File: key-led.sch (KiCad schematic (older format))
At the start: 8 parts, among them J1 Conn_01x01_Female, J2 Conn_01x01_Female, J3 Conn_01x01_Female, J4 Conn_01x01_Female, J5 Conn_01x01_Female, J6 Conn_01x01_Female, SW1 SW_Push_45deg

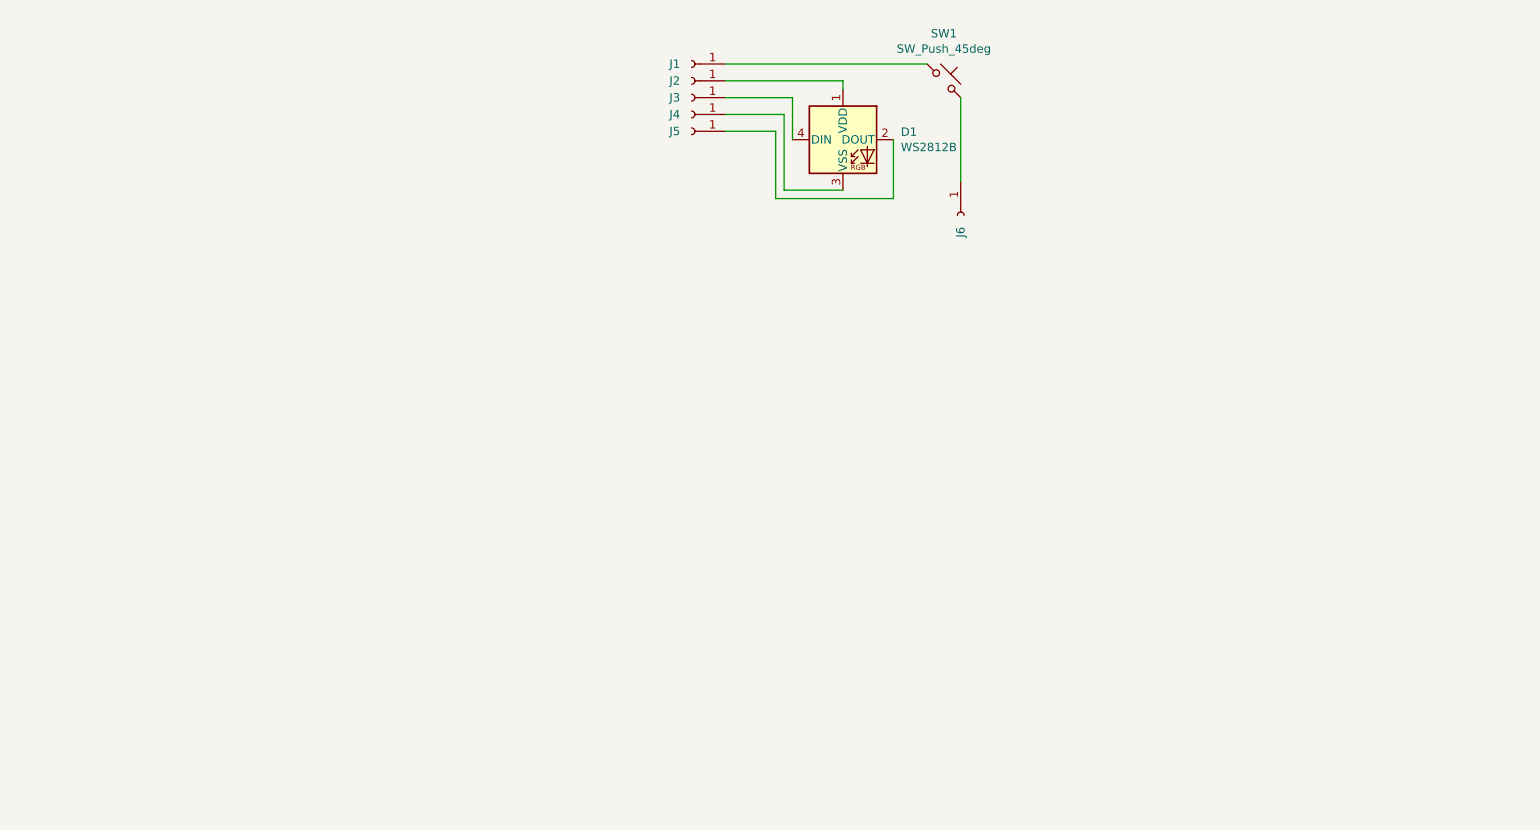
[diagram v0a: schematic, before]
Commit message: 4x row design, layout and route
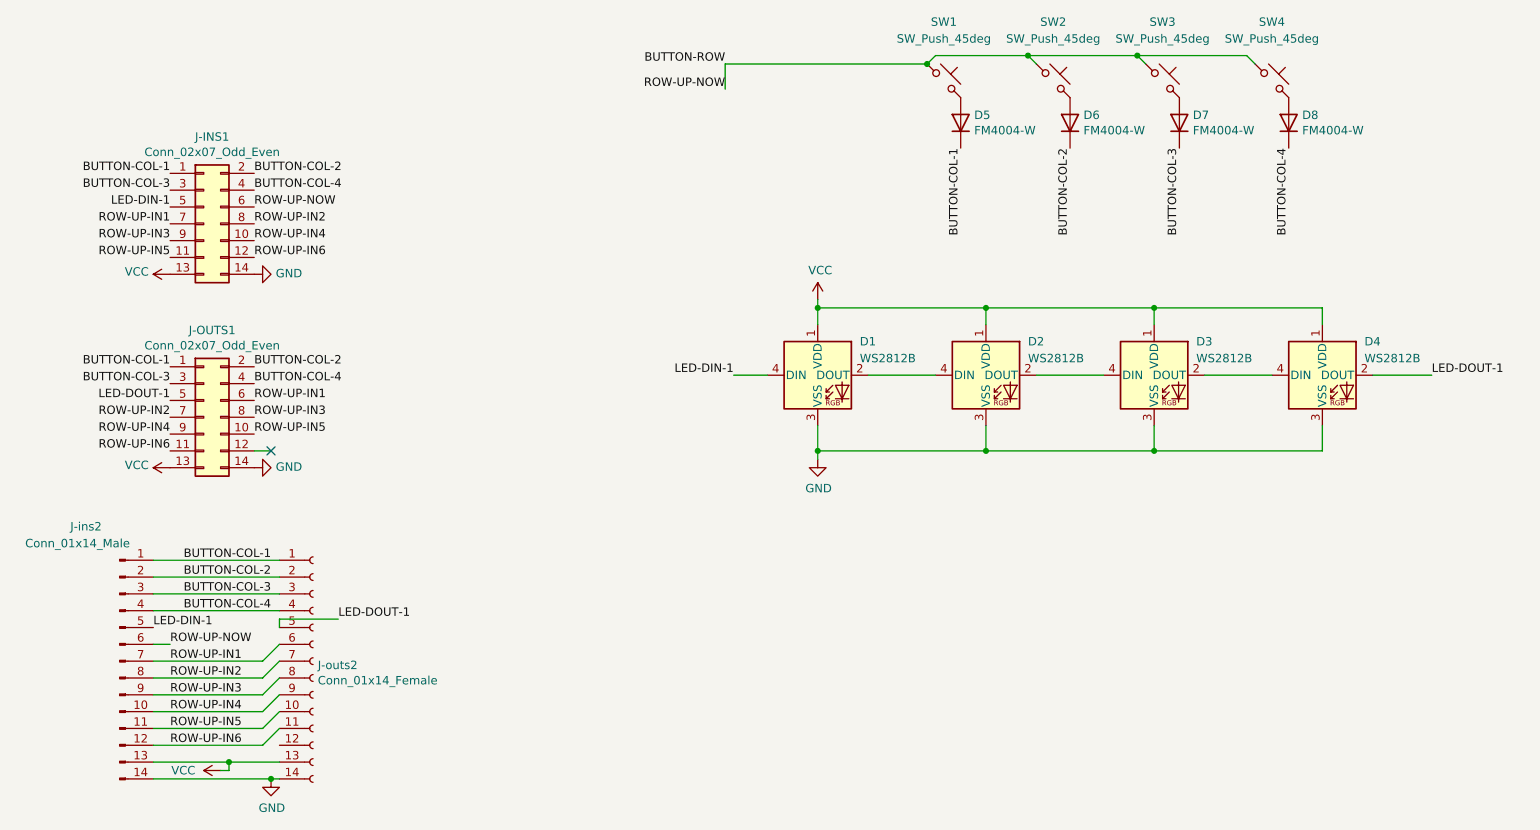
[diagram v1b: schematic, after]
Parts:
- removed J1, J2, J3, J4, J5, J6: Conn_01x01_Female, Connector_Pin:Pin_D0.9mm_L10.0mm_W2.4mm_FlatFork, symbol Connector:Conn_01x01_Female
- added D2, D3, D4: WS2812B, key-led:LED_WS2812B_PLCC4-back-mount, symbol LED:WS2812B
- added D5, D6, D7, D8: FM4004-W, Diode_SMD:D_SMA_Handsoldering, symbol Device:D
- added J-INS1, J-OUTS1: Conn_02x07_Odd_Even, Connector_PinHeader_2.54mm:PinHeader_2x07_P2.54mm_Vertical, symbol Connector_Generic:Conn_02x07_Odd_Even
- added J-ins2: Conn_01x14_Male, Connector_PinHeader_2.54mm:PinHeader_1x14_P2.54mm_Vertical, symbol Connector:Conn_01x14_Male
- added J-outs2: Conn_01x14_Female, Connector_PinHeader_2.54mm:PinHeader_1x14_P2.54mm_Vertical, symbol Connector:Conn_01x14_Female
- added SW2, SW3, SW4: SW_Push_45deg, key-led:SW_Cherry_MX_1.00u_PCB, symbol Switch:SW_Push_45deg
- D1: footprint LED_SMD:LED_WS2812B_PLCC4_5.0x5.0mm_P3.2mm -> key-led:LED_WS2812B_PLCC4-back-mount; buy link (none) -> https://www.ebay.com/itm/WS2812B-5050-SMD-Individually-Addr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
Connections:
- net VCC: now reaches D1.1 (VDD)
- net VCC: now also D2.1 (VDD), D3.1 (VDD), D4.1 (VDD), J-INS1.13 (Pin_13), J-OUTS1.13 (Pin_13), J-ins2.13 (Pin_13), J-outs2.13 (Pin_13)
- net at D1.2 (DOUT): now also D2.4 (DIN)
- net GND: now reaches D1.3 (VSS)
- net GND: now also D2.3 (VSS), D3.3 (VSS), D4.3 (VSS), J-INS1.14 (Pin_14), J-OUTS1.14 (Pin_14), J-ins2.14 (Pin_14), J-outs2.14 (Pin_14)
- net LED-DIN-1: now reaches D1.4 (DIN)
- net LED-DIN-1: now also J-INS1.5 (Pin_5), J-ins2.5 (Pin_5)
- net BUTTON-ROW: now reaches SW1.1
- net BUTTON-ROW: now also J-INS1.6 (Pin_6), J-ins2.6 (Pin_6), SW2.1, SW3.1, SW4.1
- net at SW1.2: now also D5.2 (A)
- new net: D6.2 (A), SW2.2
- new net: D7.2 (A), SW3.2
- new net: D8.2 (A), SW4.2
- new net: D2.2 (DOUT), D3.4 (DIN)
- new net: D3.2 (DOUT), D4.4 (DIN)
- new net BUTTON-COL-1: D5.1 (K), J-INS1.1 (Pin_1), J-OUTS1.1 (Pin_1), J-ins2.1 (Pin_1), J-outs2.1 (Pin_1)
- new net BUTTON-COL-2: D6.1 (K), J-INS1.2 (Pin_2), J-OUTS1.2 (Pin_2), J-ins2.2 (Pin_2), J-outs2.2 (Pin_2)
- new net BUTTON-COL-3: D7.1 (K), J-INS1.3 (Pin_3), J-OUTS1.3 (Pin_3), J-ins2.3 (Pin_3), J-outs2.3 (Pin_3)
- new net BUTTON-COL-4: D8.1 (K), J-INS1.4 (Pin_4), J-OUTS1.4 (Pin_4), J-ins2.4 (Pin_4), J-outs2.4 (Pin_4)
- new net LED-DOUT-1: D4.2 (DOUT), J-OUTS1.5 (Pin_5), J-outs2.5 (Pin_5)
- new net ROW-UP-IN1: J-INS1.7 (Pin_7), J-OUTS1.6 (Pin_6), J-ins2.7 (Pin_7), J-outs2.6 (Pin_6)
- new net ROW-UP-IN2: J-INS1.8 (Pin_8), J-OUTS1.7 (Pin_7), J-ins2.8 (Pin_8), J-outs2.7 (Pin_7)
- new net ROW-UP-IN3: J-INS1.9 (Pin_9), J-OUTS1.8 (Pin_8), J-ins2.9 (Pin_9), J-outs2.8 (Pin_8)
- new net ROW-UP-IN4: J-INS1.10 (Pin_10), J-OUTS1.9 (Pin_9), J-ins2.10 (Pin_10), J-outs2.9 (Pin_9)
- new net ROW-UP-IN5: J-INS1.11 (Pin_11), J-OUTS1.10 (Pin_10), J-ins2.11 (Pin_11), J-outs2.10 (Pin_10)
- new net ROW-UP-IN6: J-INS1.12 (Pin_12), J-OUTS1.11 (Pin_11), J-ins2.12 (Pin_12), J-outs2.11 (Pin_11)
- no-connect marks 0 -> 1
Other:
- moved on the sheet: D1
